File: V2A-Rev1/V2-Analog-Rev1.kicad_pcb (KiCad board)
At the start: 4 copper layers, 106.3 x 56.7 mm, 36 parts, among them J1 Apple II, J2 DB15_Female_HighDensity_Mount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, J3 NOPAL, U1 SN74LVC8T245DGVR, U2 SN74LVC8T245DGVR, U3 SN74LVC8T245DGVR, U4 SN74LVC8T245DGVR, U5 PALCE16V8H-5JC/5, U6 Pi PICO, U7 AZ1117I-H-3.3

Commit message: My reinterpretation of V2RetroComputing's Analog VGA Board.
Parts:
- added J4: NOWIFI, Jumper:SolderJumper-2_P1.3mm_Open_TrianglePad1.0x1.5mm, B.Cu at (159.2, 90.1)
- added J5: VGA, Connector_PinHeader_2.54mm:PinHeader_2x08_P2.54mm_Vertical, F.Cu at (99.4, 121.4)
- added J6: VGA, Connector_PinHeader_2.54mm:PinHeader_2x08_P2.54mm_Vertical, F.Cu at (108.3, 121.4)
- C1, C2, C3, C4, C5, C6, C7, C8, C9: value C -> 0.1uF
- J3: moved to B.Cu
- R12, R13, R14: footprint Resistor_SMD:R_0402_1005Metric_Pad0.72x0.64mm_HandSolder -> Resistor_SMD:R_0603_1608Metric_Pad0.98x0.95mm_HandSolder
- U6: value Pi PICO -> Pi PICO W
- moved R10 23.0 mm to (115.3, 117.6)
- moved R11 22.8 mm to (115.3, 118.8)
- moved R2 18.6 mm to (115.3, 108.7)
- moved R1 18.6 mm to (115.3, 110.2)
- moved R3 18.6 mm to (115.3, 107.1)
- moved R4 18.6 mm to (115.3, 105.1)
- moved R5 18.6 mm to (115.3, 103.6)
- moved R6 18.6 mm to (115.3, 102.1)
- moved R7 18.1 mm to (115.3, 115.5)
- moved R8 18.1 mm to (115.3, 114.0)
- moved R9 18.1 mm to (115.3, 112.5)
- moved C1 5.59 mm to (128.9, 116.7)
- moved C2 5.59 mm to (128.9, 111.0)
- moved U1 5.59 mm to (123.2, 113.9)
- moved C3 4.19 mm to (138.9, 116.7)
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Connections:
- J1 pad 19: Net-(J1-Pad19) -> unconnected-(J1-Pad19)
- J1 pad 35: Net-(J1-Pad35) -> unconnected-(J1-Pad35)
- J2 pad 11: Net-(J2-Pad11) -> unconnected-(J2-Pad11)
- J2 pad 12: Net-(J2-Pad12) -> unconnected-(J2-Pad12)
- J2 pad 15: Net-(J2-Pad15) -> unconnected-(J2-Pad15)
- J2 pad 4: Net-(J2-Pad4) -> unconnected-(J2-Pad4)
- J2 pad 9: Net-(J2-Pad9) -> unconnected-(J2-Pad9)
- U4 pad 3: Net-(U4-Pad3) -> unconnected-(U4-Pad3)
- U4 pad 4: Net-(U4-Pad4) -> unconnected-(U4-Pad4)
- U4 pad 5: Net-(U4-Pad5) -> unconnected-(U4-Pad5)
- U4 pad 6: Net-(U4-Pad6) -> unconnected-(U4-Pad6)
- U5 pad 1: Net-(U5-Pad1) -> unconnected-(U5-Pad1)
- U5 pad 15: Net-(U5-Pad15) -> unconnected-(U5-Pad15)
- U5 pad 16: Net-(U5-Pad16) -> unconnected-(U5-Pad16)
- U5 pad 17: Net-(U5-Pad17) -> unconnected-(U5-Pad17)
- U5 pad 18: Net-(U5-Pad18) -> unconnected-(U5-Pad18)
- U5 pad 19: Net-(U5-Pad19) -> unconnected-(U5-Pad19)
- U6 pad 30: Net-(U6-Pad30) -> nonWiFi
- U6 pad 35: Net-(U6-Pad35) -> unconnected-(U6-Pad35)
- U6 pad 36: Net-(U6-Pad36) -> unconnected-(U6-Pad36)
- U6 pad 37: Net-(U6-Pad37) -> unconnected-(U6-Pad37)
- U6 pad 40: Net-(U6-Pad40) -> unconnected-(U6-Pad40)
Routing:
- net GND: track 181.3 -> 299.4 mm, vias 44 -> 45
- net VSYNC_OUT: track 14.2 -> 44.7 mm
- net GREEN_OUT: track 11.1 -> 37.2 mm
- net nMSBOE: track 46.1 -> 71.5 mm
- net RED_OUT: track 12.8 -> 37.3 mm, vias 0 -> 1
- net HSYNC_OUT: track 16.1 -> 40.1 mm, vias 1 -> 0
- net R1: track 87.0 -> 66.5 mm
- net G1: track 90.6 -> 70.4 mm
- net R0: track 82.8 -> 62.8 mm
- net G2: track 95.1 -> 75.0 mm
- net R2: track 88.0 -> 68.0 mm
- net G0: track 88.8 -> 69.4 mm
- net BLUE_OUT: track 13.1 -> 32.4 mm
- net LD7: track 69.0 -> 59.2 mm
- net LD6: track 66.0 -> 56.3 mm
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- removed copper zone on In1.Cu, net GND
- removed copper zone on In2.Cu, net GND
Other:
- outline, holes or cut-outs redrawn
- copper layers 4 -> 2
- net class Default removed
- board text added: "Board Design by Aaron Yourk Copyright c 2023 Based on Apple II VGA by Mark Aikens, David Kuder, & Hans Hübner"
- board text added: "Rev 1ay"
- board text added: "∀2"
- board text removed: "Board Design by David Kuder Copyright c 2022 Based on Apple II VGA by Mark Aikens"
- board text removed: "Rev 1"
- board text removed: "V2"

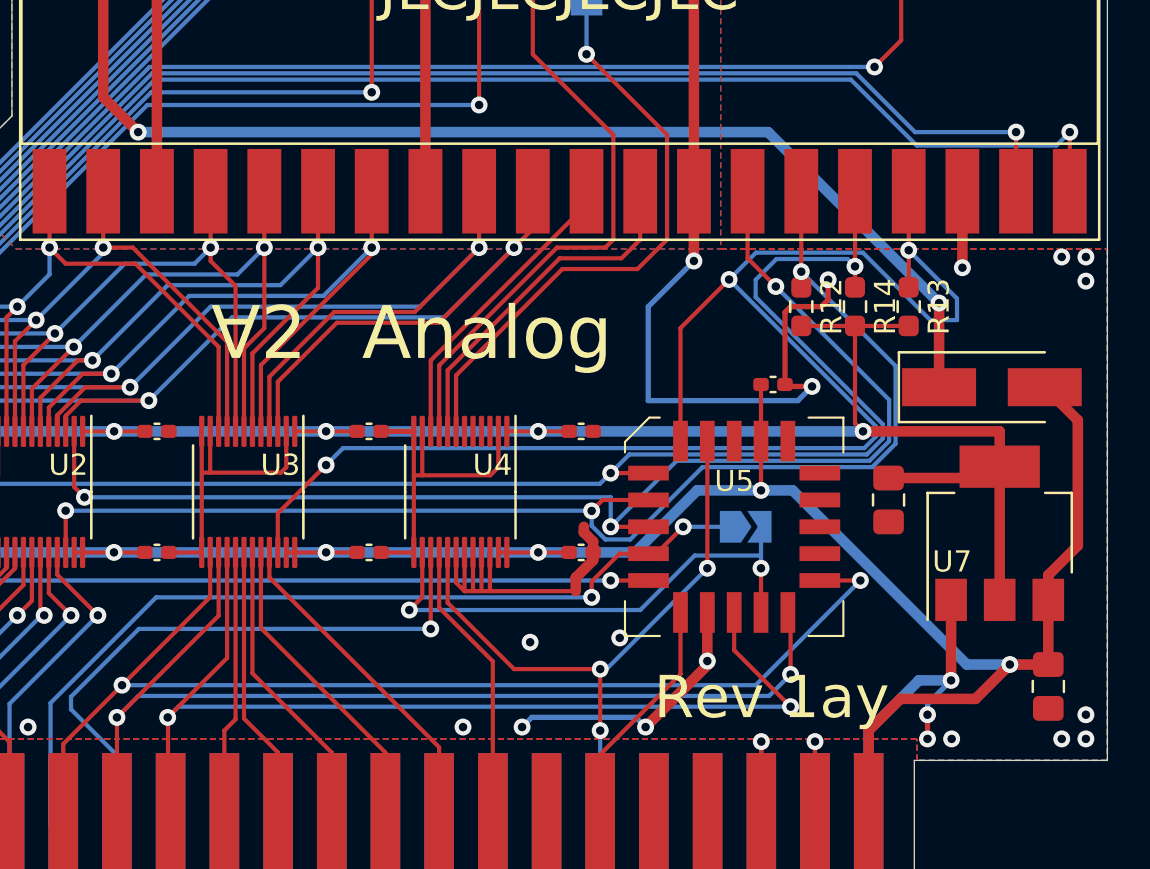
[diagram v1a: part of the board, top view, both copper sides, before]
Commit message: Update design to use a PLCC socket for PAL/GAL.
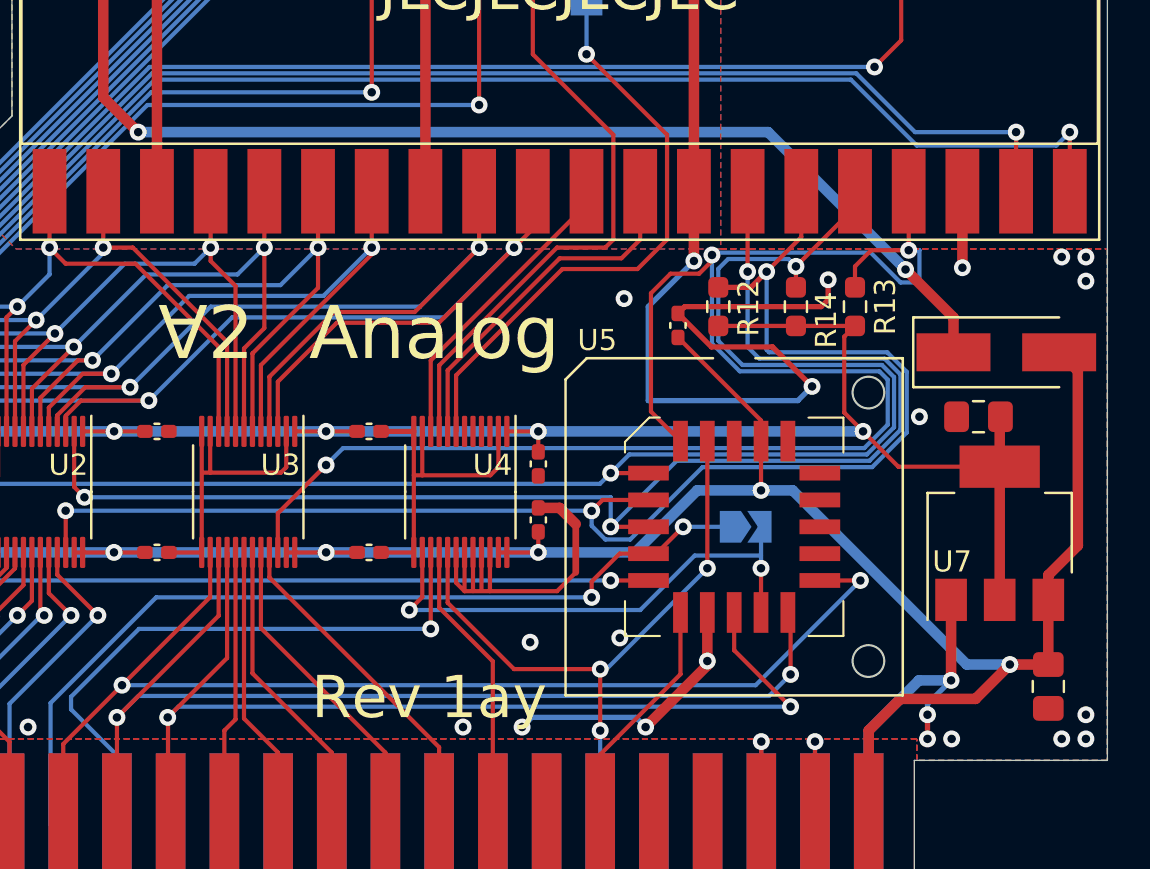
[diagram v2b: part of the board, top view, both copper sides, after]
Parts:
- added BP1: PALCE16V8H-5JC/5, V2-Analog-Rev1:BOM_Placeholder, F.Cu at (166.2, 115.5)
- J3: value NOPAL -> NOPAL/GAL
- U5: value PALCE16V8H-5JC/5 -> PLCC Socket; footprint Package_LCC:PLCC-20 -> V2-Analog-Rev1:A-CCS 020-Z-SM_SMD-Socket
- moved C10 5.80 mm to (177.8, 110.3), turned to 180 degrees
- moved C9 5.29 mm to (163.6, 106.0), turned to 90 degrees
- moved R12 3.93 mm to (165.5, 105.1)
- moved R14 2.79 mm to (169.1, 105.1)
- moved C8 2.54 mm to (157.0, 112.6), turned to -90 degrees
- moved C7 2.54 mm to (157.0, 115.2), turned to 90 degrees
- moved R13 2.54 mm to (171.9, 105.1)
- moved D1 1.79 mm to (179.1, 107.3)
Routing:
- net GND: track 299.4 -> 308.7 mm, vias 45 -> 47
- net nDATAOE: track 61.0 -> 67.9 mm
- net nMSBOE: track 71.5 -> 77.8 mm
- net nLSBOE: track 73.2 -> 78.7 mm
- net +5V: track 104.7 -> 109.4 mm
- net nDATADIR: track 60.3 -> 64.2 mm
- net +3V3: track 87.2 -> 83.9 mm
- net Net-(D1-Pad1): track 62.9 -> 61.5 mm

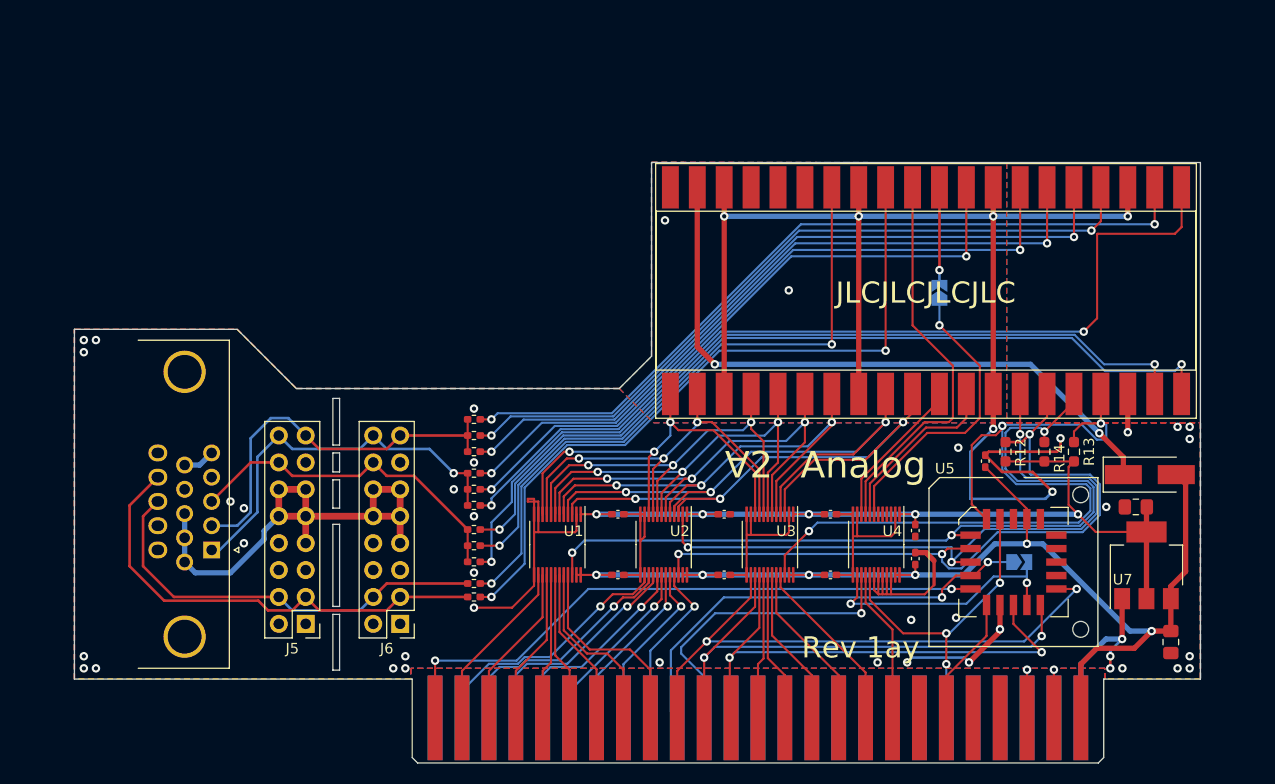
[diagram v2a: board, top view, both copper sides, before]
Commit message: Added socket for PLCC. Reorganized layout for improved VGA picture clarity.
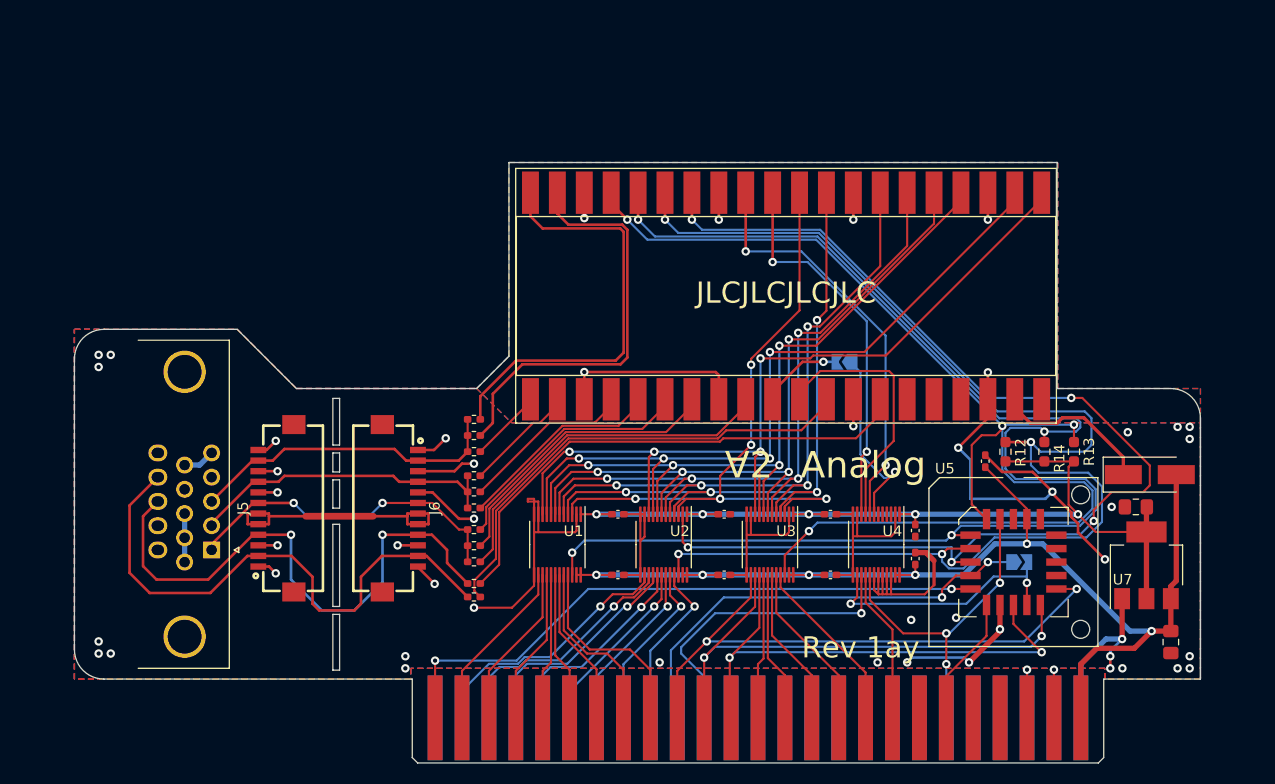
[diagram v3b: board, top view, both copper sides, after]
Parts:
- added BP2: FPC 12pin 1.0mm pitch, V2-Analog-Rev1:BOM_Placeholder, F.Cu at (99.3, 129.9)
- J2: footprint Connector_Dsub:DSUB-15-HD_Female_Horizontal_P2.29x1.98mm_EdgePinOffset3.03mm_Housed_MountingHolesOffset4.94mm -> V2-Analog-Rev1:DSUB-15-HD_Female_Horizontal_P2.29x1.98mm_EdgePinOffset3.03mm_Housed_MountingHolesOffset4.94mm
- J4: value NOWIFI -> NONWIFI
- J5, J6: footprint Connector_PinHeader_2.54mm:PinHeader_2x08_P2.54mm_Vertical -> V2-Analog-Rev1:FPC-SMD_12P-P1.00_FH12-12S-1SH
- U5: footprint V2-Analog-Rev1:A-CCS 020-Z-SM_SMD-Socket -> V2-Analog-Rev1:A-CCS_020-Z-SM_SMD-Socket
- moved U6 13.7 mm to (144.8, 88.4), turned to -90 degrees
- moved R8 11.9 mm to (115.3, 102.1)
- moved J5 11.3 mm to (96.6, 110.4), turned to 90 degrees
- moved J4 11.1 mm to (150.3, 96.6), turned to 180 degrees
- moved J6 10.9 mm to (108.3, 110.4), turned to -90 degrees
- moved R7 10.4 mm to (115.3, 105.1)
- moved R9 8.88 mm to (115.3, 103.6)
- moved R1 5.32 mm to (115.3, 115.5)
- moved R2 5.32 mm to (115.3, 114.0)
- moved R4 5.32 mm to (115.3, 110.4)
- moved R5 5.32 mm to (115.3, 108.9)
- moved R6 5.32 mm to (115.3, 107.4)
- moved R3 5.32 mm to (115.3, 112.5)
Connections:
- J5 pad 1: unconnected-(J5-Pad1) -> GND
- J5 pad 11: GND -> BLUE_OUT
- J5 pad 13: unconnected-(J5-Pad13) -> GND
- J5 pad 14: BLUE_OUT -> GND
- J5 pad 2: unconnected-(J5-Pad2) -> VSYNC_OUT
- J5 pad 3: VSYNC_OUT -> GND
- J5 pad 5: unconnected-(J5-Pad5) -> GND
- J5 pad 6: unconnected-(J5-Pad6) -> GND
- J5 pad 7: GND -> RED_OUT
- J5 pad 8: unconnected-(J5-Pad8) -> GND
- J5 pad 9: GND -> GREEN_OUT
- J6 pad 1: unconnected-(J6-Pad1) -> GND
- J6 pad 11: GND -> VSYNC_OUT
- J6 pad 13: unconnected-(J6-Pad13) -> GND
- J6 pad 14: BLUE_OUT -> GND
- J6 pad 2: unconnected-(J6-Pad2) -> BLUE_OUT
- J6 pad 3: VSYNC_OUT -> GND
- J6 pad 4: HSYNC_OUT -> GREEN_OUT
- J6 pad 5: unconnected-(J6-Pad5) -> GND
- J6 pad 6: unconnected-(J6-Pad6) -> RED_OUT
- J6 pad 8: unconnected-(J6-Pad8) -> GND
- J6 pad 9: GND -> HSYNC_OUT
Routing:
- net B0: track 91.2 -> 6.91 mm, vias 2 -> 0
- net G2: track 75.0 -> 10.6 mm, vias 2 -> 0
- net GND: track 308.7 -> 247.3 mm, vias 47 -> 48
- net nDATAOE: track 67.9 -> 122.6 mm, vias 3 -> 4
- net G1: track 70.4 -> 16.4 mm, vias 2 -> 0
- net nLSBOE: track 78.7 -> 131.0 mm, vias 3 -> 4
- net G0: track 69.4 -> 19.5 mm, vias 2 -> 0
- net nDATADIR: track 64.2 -> 111.0 mm, vias 3 -> 5
- net Net-(D1-Pad1): track 61.5 -> 15.0 mm, vias 2 -> 0
- net R2: track 68.0 -> 23.8 mm, vias 2 -> 0
- net B1: track 81.5 -> 40.4 mm, vias 2 -> 0
- net R1: track 66.5 -> 27.6 mm, vias 2 -> 0
- net LD0: track 40.9 -> 79.7 mm, vias 3 -> 4
- net B2: track 77.4 -> 39.8 mm, vias 2 -> 0
- net LD1: track 39.7 -> 76.5 mm, vias 3 -> 4
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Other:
- outline, holes or cut-outs redrawn

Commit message: Added Left and Right Fiducial break away Rails
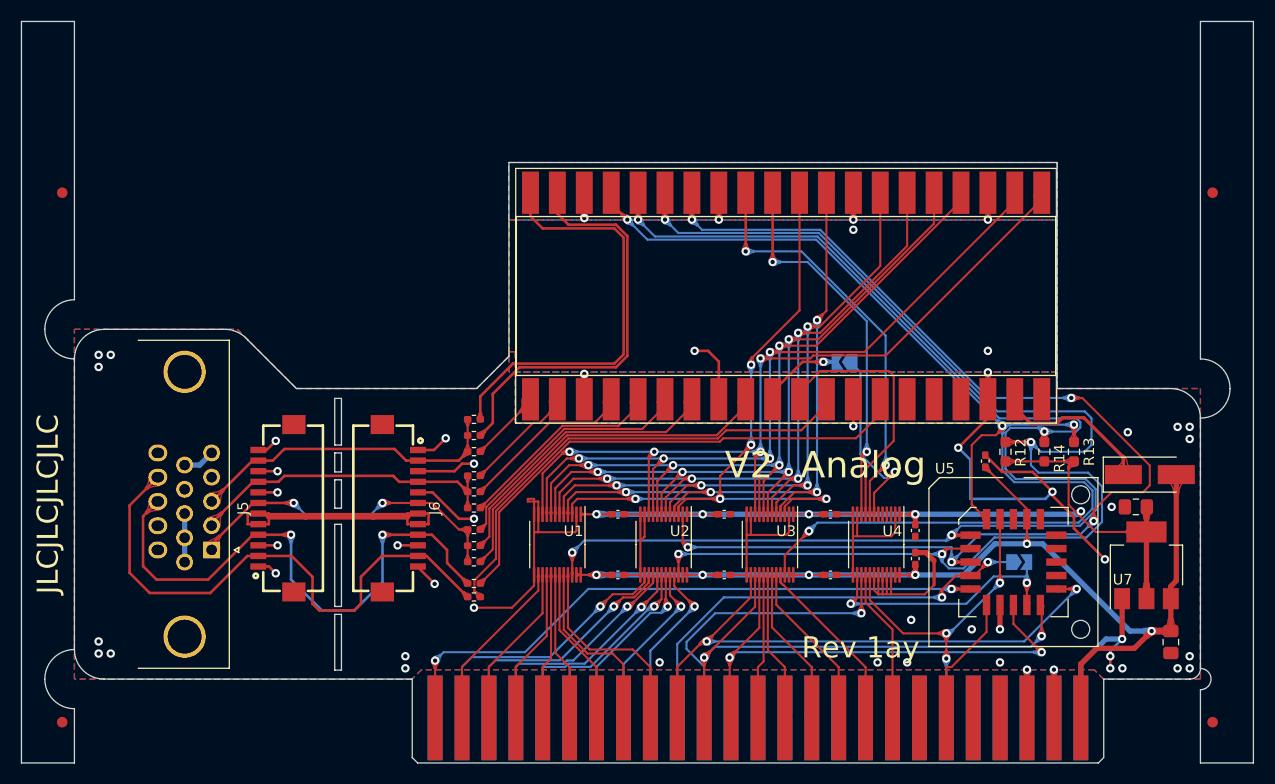
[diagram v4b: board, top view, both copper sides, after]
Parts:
- added REF**: Fiducial_1mm_Mask2mm, Fiducial:Fiducial_1mm_Mask2mm, F.Cu at (185.0, 80.7)
- added REF**: Fiducial_1mm_Mask2mm, Fiducial:Fiducial_1mm_Mask2mm, F.Cu at (76.4, 80.7)
- added REF**: Fiducial_1mm_Mask2mm, Fiducial:Fiducial_1mm_Mask2mm, F.Cu at (76.4, 130.6)
- added REF**: Fiducial_1mm_Mask2mm, Fiducial:Fiducial_1mm_Mask2mm, F.Cu at (185.0, 130.6)
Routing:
- net GND: track 247.3 -> 227.7 mm, vias 48 -> 51
- net D4: track 17.1 -> 18.4 mm
- net D0: track 24.7 -> 26.1 mm
- net +3V3: track 84.6 -> 85.4 mm
- net D1: track 23.3 -> 23.9 mm
- net D5: track 16.4 -> 17.0 mm
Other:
- board size 106.3 x 56.7 mm -> 116.3 x 70 mm

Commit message: Fix issues with JLCPCB manufacturing standards.
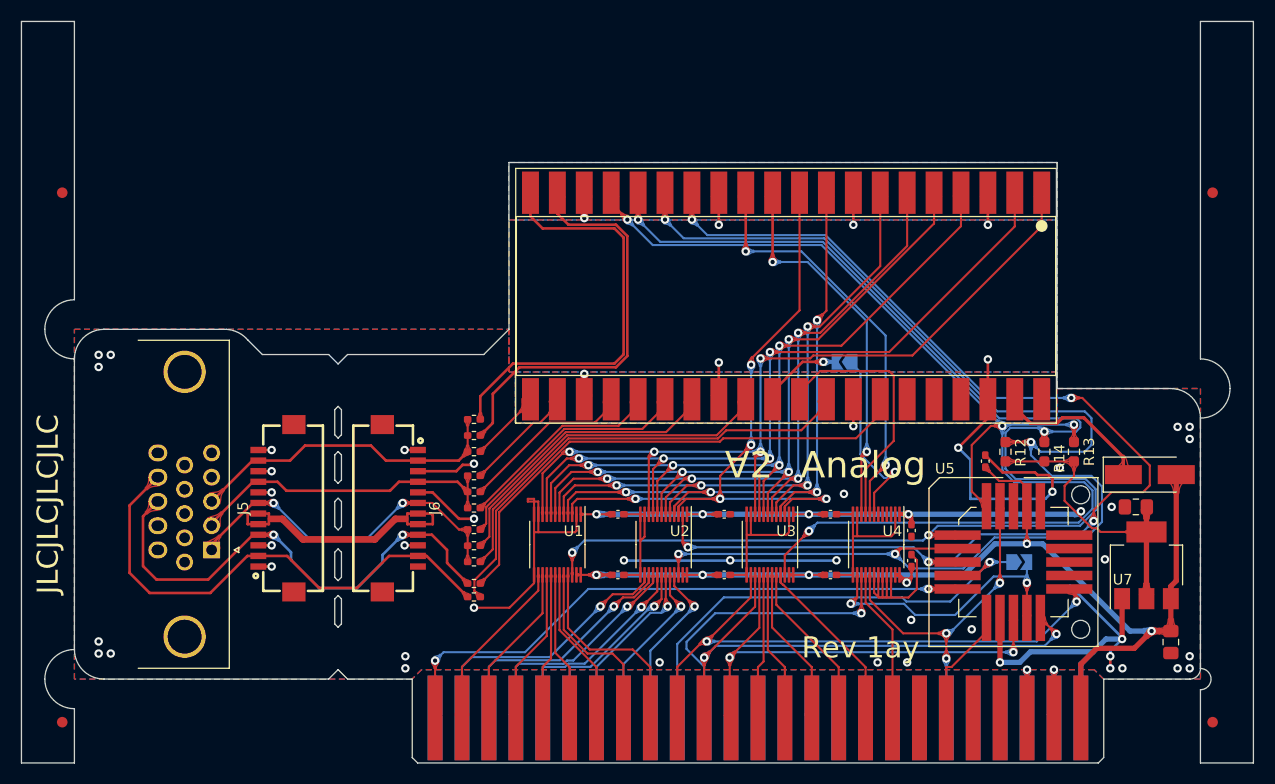
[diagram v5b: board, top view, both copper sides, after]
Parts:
- moved C7 0.41 mm to (156.6, 115.4)
- moved C8 0.36 mm to (156.6, 112.6)
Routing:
- net GND: track 227.7 -> 243.3 mm
- net HSYNC_OUT: track 53.2 -> 47.2 mm
- net A10: track 49.9 -> 45.0 mm
- net VSYNC_OUT: track 53.1 -> 48.4 mm
- net nDEVSEL: track 42.2 -> 45.8 mm, vias 2 -> 1
- net nDATAOE: track 122.6 -> 124.8 mm
- net +5V: track 108.7 -> 110.8 mm
- net nCARDSEL: track 24.7 -> 26.8 mm
- net RED_OUT: track 31.4 -> 33.3 mm
- net LD0: track 79.7 -> 81.2 mm
- net LD2: track 70.5 -> 71.9 mm
- net nMSBOE: track 114.4 -> 113.0 mm
- net LD1: track 76.5 -> 77.8 mm
- net nSYSRESET: track 31.9 -> 33.2 mm
- net nIOSTROBE: track 12.5 -> 11.3 mm
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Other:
- outline, holes or cut-outs redrawn
- board text added: "Pin 1"
